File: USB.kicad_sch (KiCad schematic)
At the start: 37 parts, among them J1 USB_C_Receptacle_USB2.0_16P, U6 93AAxxBT-xOT, U7 USBLC6-2SC6, U8 FT4232H, Y2 Crystal_GND24

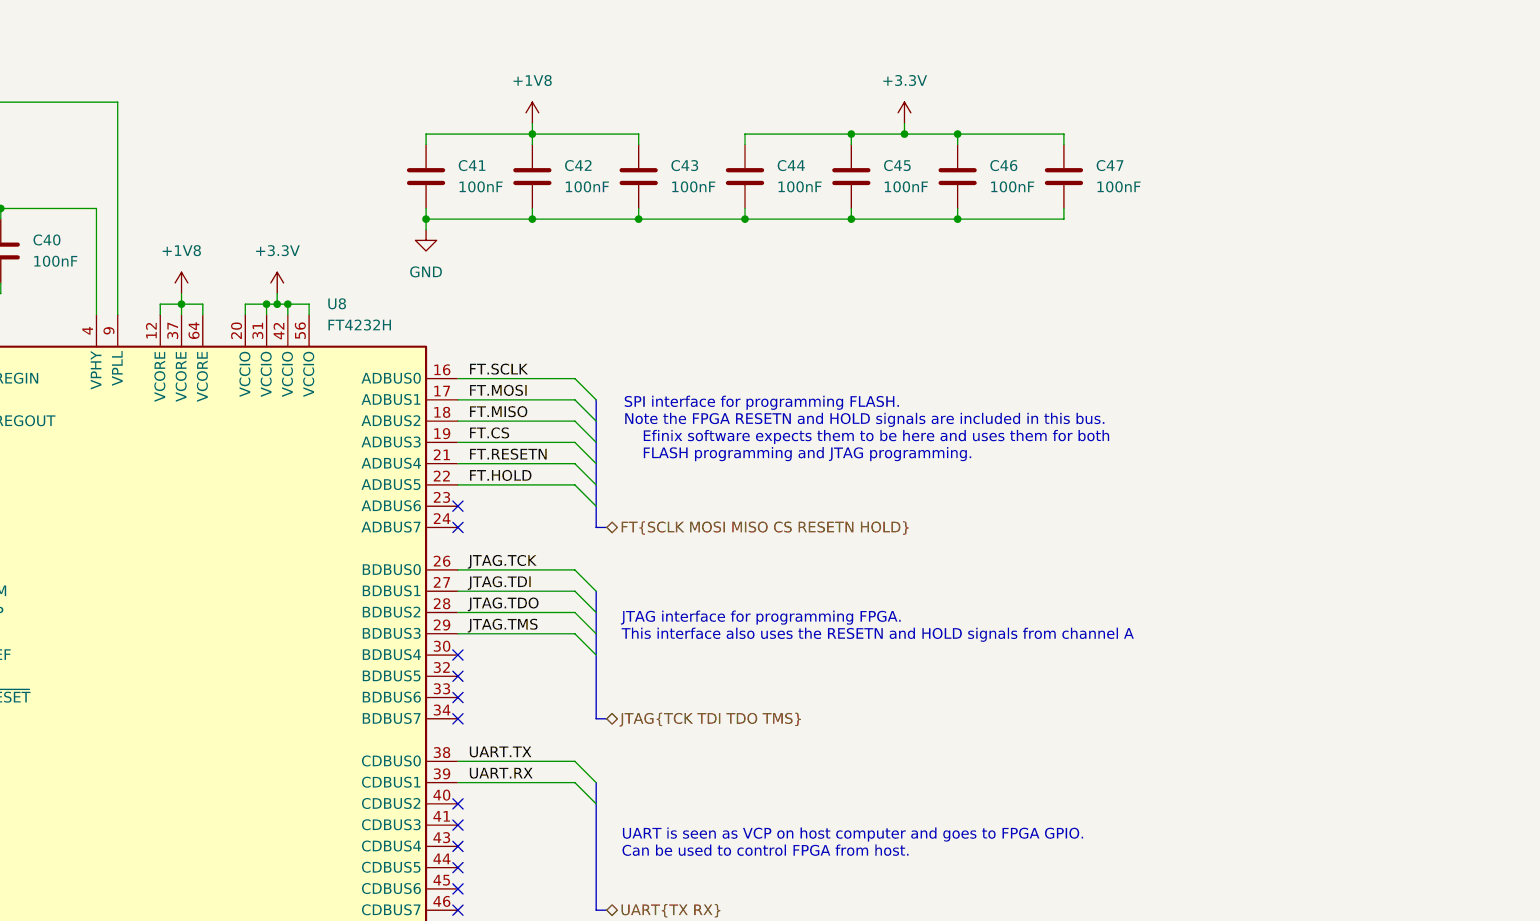
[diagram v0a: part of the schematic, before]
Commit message: Added SPI bus buffer
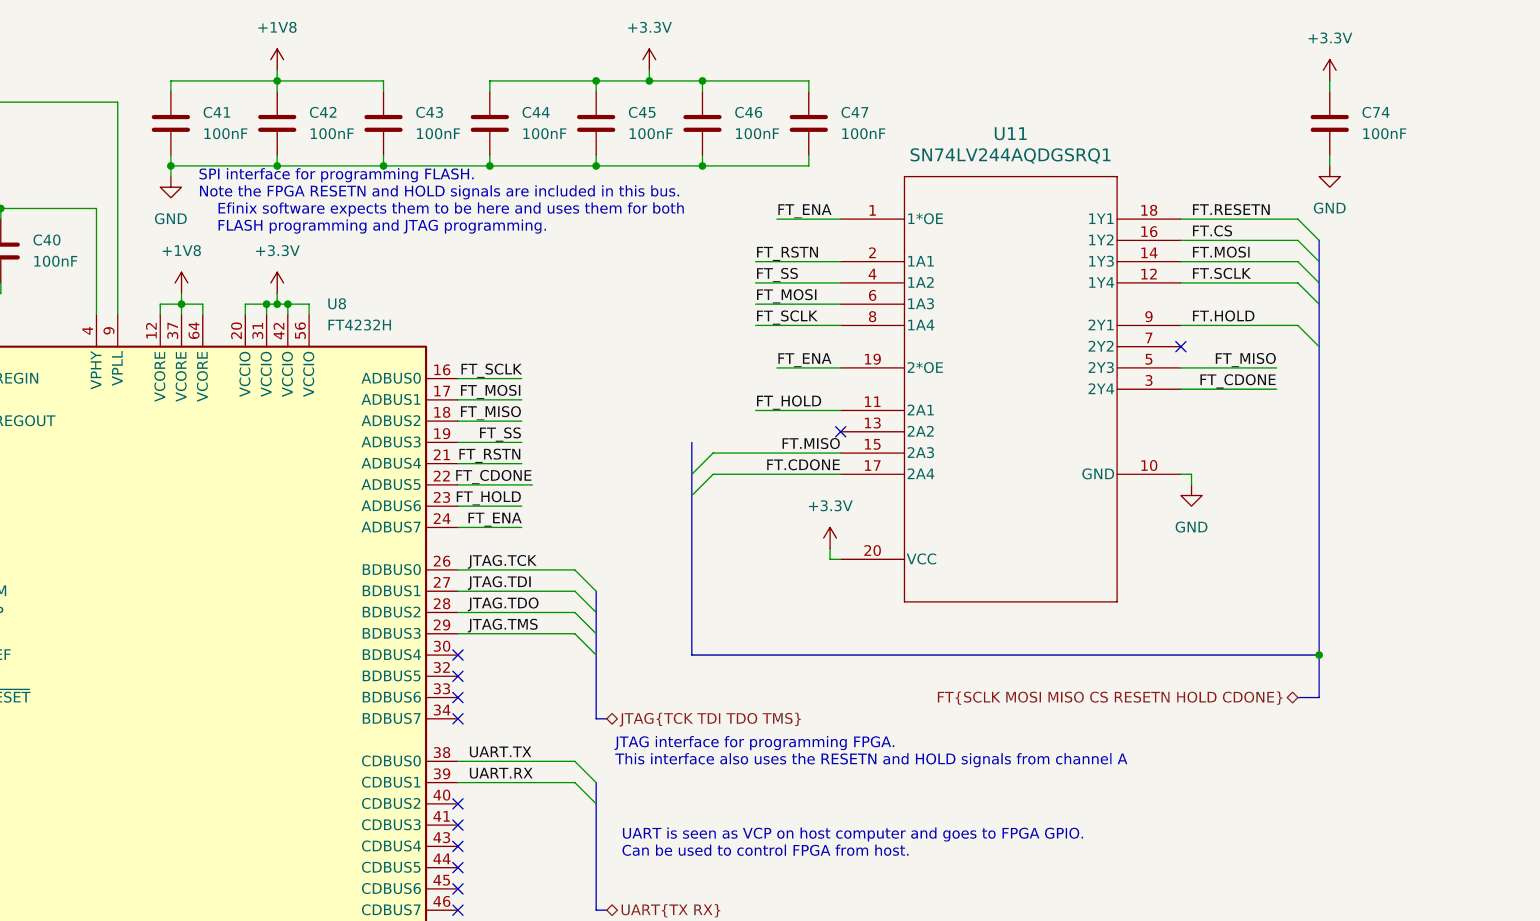
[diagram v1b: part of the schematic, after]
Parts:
- added C74: 100nF, Capacitor_SMD:C_0603_1608Metric, symbol Device:C
- added U11: SN74LV244AQDGSRQ1, SN74LV244AQDGSRQ1:VSSOP20_DGS_TEX, symbol SN74LV244AQDGSRQ1:SN74LV244AQDGSRQ1
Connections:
- net +3.3V: now also C74.1, U11.20 (VCC)
- net FT.CS: now also U11.16 (1Y2); no longer U8.19 (ADBUS3)
- net FT.HOLD: now also U11.9 (2Y1); no longer U8.22 (ADBUS5)
- net FT.MISO: now also U11.15 (2A3); no longer U8.18 (ADBUS2)
- net FT.MOSI: now also U11.14 (1Y3); no longer U8.17 (ADBUS1)
- net FT.RESETN: now also U11.18 (1Y1); no longer U8.21 (ADBUS4)
- net FT.SCLK: now also U11.12 (1Y4); no longer U8.16 (ADBUS0)
- net GND: now also C74.2, U11.10 (GND)
- net FT_HOLD: now reaches U8.23 (ADBUS6)
- net FT_HOLD: now also U11.11 (2A1)
- net FT_ENA: now reaches U8.24 (ADBUS7)
- net FT_ENA: now also U11.1 (1*OE), U11.19 (2*OE)
- new net FT.CDONE: U11.17 (2A4)
- new net FT_CDONE: U11.3 (2Y4), U8.22 (ADBUS5)
- new net FT_MISO: U11.5 (2Y3), U8.18 (ADBUS2)
- new net FT_MOSI: U11.6 (1A3), U8.17 (ADBUS1)
- new net FT_RSTN: U11.2 (1A1), U8.21 (ADBUS4)
- new net FT_SCLK: U11.8 (1A4), U8.16 (ADBUS0)
- new net FT_SS: U11.4 (1A2), U8.19 (ADBUS3)
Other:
- moved on the sheet: C41, C42, C43, C44, C45, C46, C47

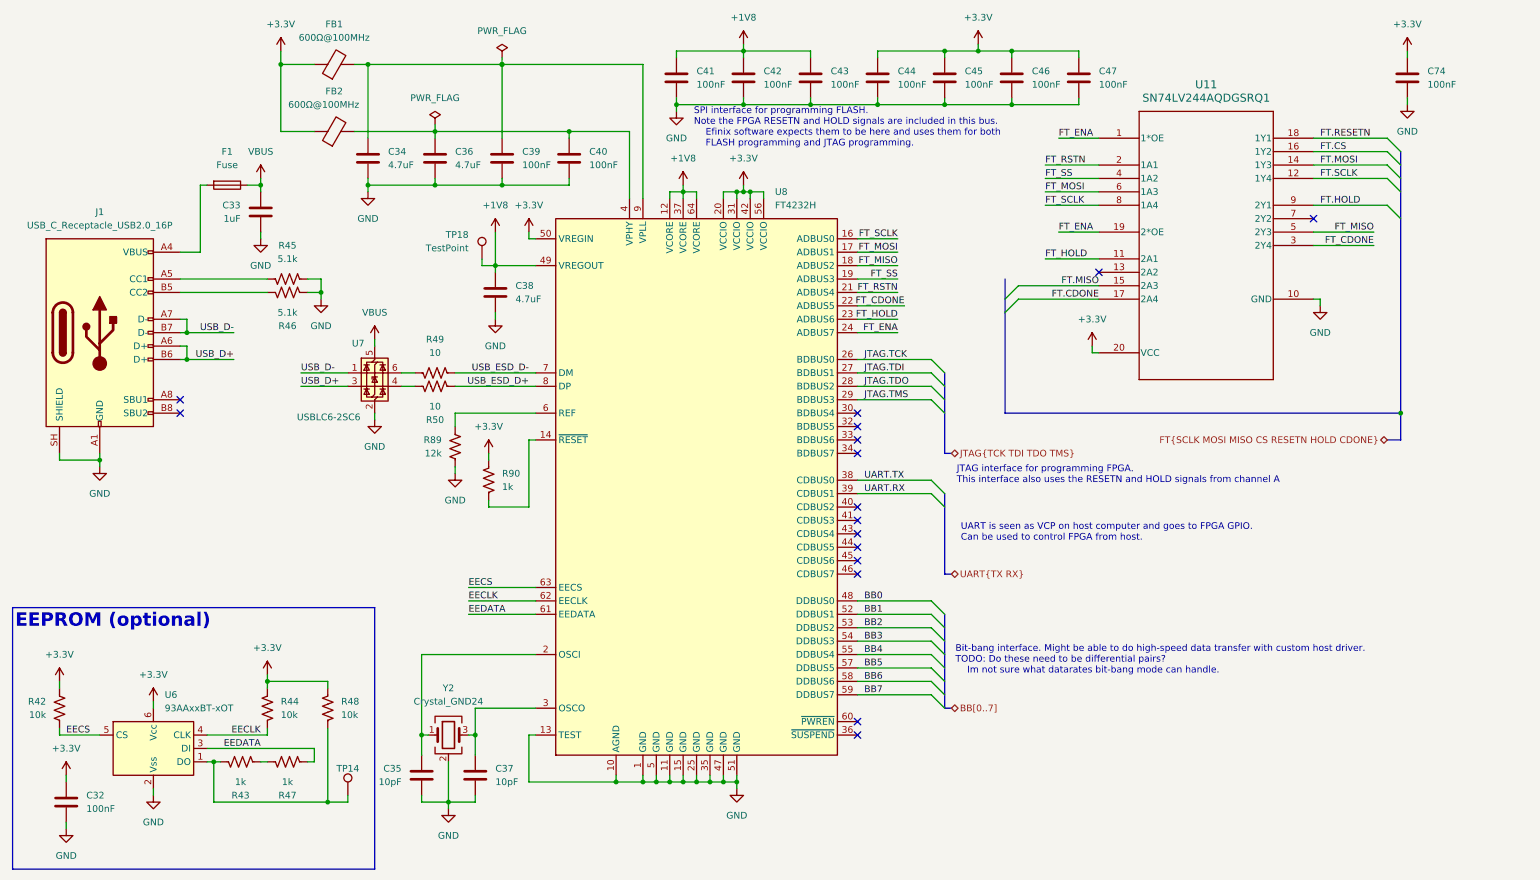
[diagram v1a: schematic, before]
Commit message: Added decal and gerbers
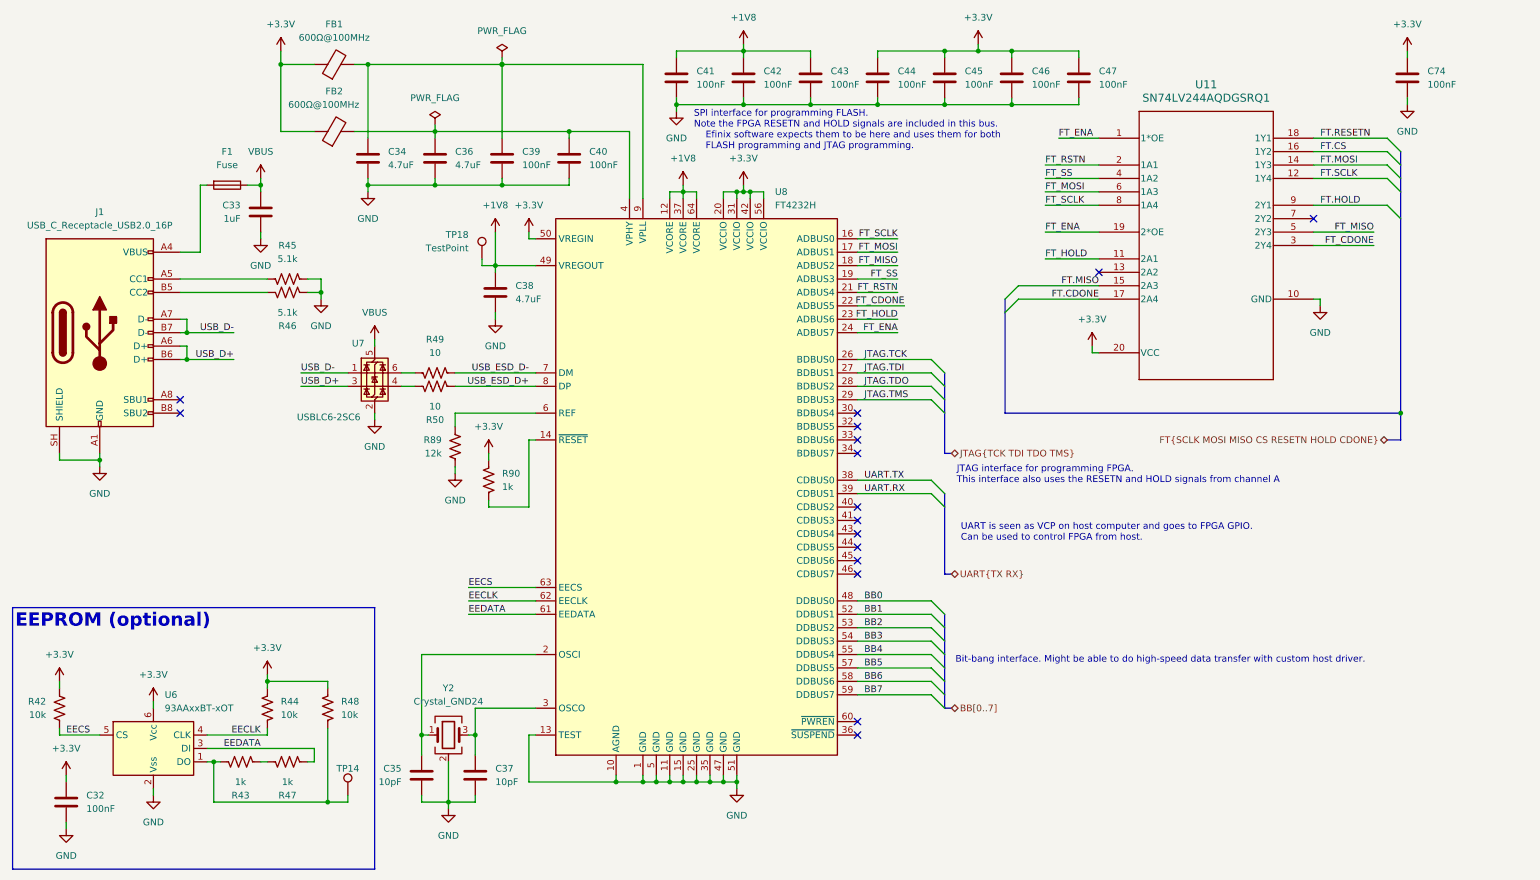
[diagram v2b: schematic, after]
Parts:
- U11: Digikey PN (none) -> 296-SN74LV244AQDGSRQ1CT-ND; Unit Cost (none) -> 0.68
- U7: Digikey PN (none) -> 497-5235-1-ND; Unit Cost (none) -> 0.54
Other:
- note added: "Bit-bang interface. Might be able to do high-speed data transfer with custom host driver."
- note removed: "Bit-bang interface. Might be able to do high-speed data transfer with custom host driver. TODO: Do these need to be differential pairs? Im not sure what datarates bit-bang mode can handle."
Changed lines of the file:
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@@
 	(text "SPI interface for programming FLASH.\nNote the FPGA RESETN and HOLD signals are included in this bus.\n	Efinix software expects them to be here and uses them for both \n	FLASH programming and JTAG programming."
 		(exclude_from_sim no)
-		(at 141.732 34.798 0)
+		(at 141.732 35.306 0)
 		(effects
 			(font
@@
 		)
 	)
-	(text "Bit-bang interface. Might be able to do high-speed data transfer with custom host driver.\nTODO: Do these need to be differential pairs? \n	Im not sure what datarates bit-bang mode can handle."
+	(text "Bit-bang interface. Might be able to do high-speed data transfer with custom host driver."
 		(exclude_from_sim no)
 		(at 191.262 135.636 0)
@@
 	(wire
 		(pts
-			(xy 80.01 22.86) (xy 105.41 22.86)
+			(xy 80.01 22.86) (xy 132.08 22.86)
 		)
 		(stroke
@@
 		)
 	)
-	(bus
+	(wire
 		(pts
-			(xy 200.66 63.5) (xy 200.66 88.9)
+			(xy 147.32 48.26) (xy 147.32 46.99)
 		)
 		(stroke
@@
 	(wire
 		(pts
-			(xy 147.32 48.26) (xy 147.32 46.99)
+			(xy 68.58 63.5) (xy 71.12 63.5)
 		)
 		(stroke
@@
 	(wire
 		(pts
-			(xy 68.58 63.5) (xy 71.12 63.5)
+			(xy 92.71 35.56) (xy 92.71 36.83)
 		)
 		(stroke
@@
 	(wire
 		(pts
-			(xy 92.71 35.56) (xy 92.71 36.83)
+			(xy 172.72 104.14) (xy 186.69 104.14)
 		)
 		(stroke
@@
 	(wire
 		(pts
-			(xy 172.72 104.14) (xy 186.69 104.14)
+			(xy 201.93 20.32) (xy 201.93 21.59)
 		)
 		(stroke
@@
 		)
 	)
-	(wire
+	(bus
 		(pts
-			(xy 201.93 20.32) (xy 201.93 21.59)
+			(xy 200.66 67.31) (xy 200.66 88.9)
 		)
 		(stroke
@@
 	(wire
 		(pts
-			(xy 210.82 54.61) (xy 218.44 54.61)
+			(xy 208.28 54.61) (xy 218.44 54.61)
 		)
 		(stroke
@@
 	(wire
 		(pts
-			(xy 105.41 22.86) (xy 132.08 22.86)
-		)
-		(stroke
-			(width 0)
-			(type default)
-		)
-	)
-	(wire
-		(pts
 			(xy 172.72 134.62) (xy 186.69 134.62)
 		)
@@
 	)
 	(label "FT_ENA"
-		(at 210.82 54.61 0)
+		(at 208.28 54.61 0)
 		(effects
 			(font
@@
 			)
 		)
+		(property "Digikey PN" "497-5235-1-ND"
+			(at 81.28 81.28 0)
+			(hide yes)
+			(show_name no)
+			(do_not_autoplace no)
+			(effects
+				(font
+					(size 1.27 1.27)
+				)
+			)
+		)
+		(property "Unit Cost" "0.54"
+			(at 81.28 81.28 0)
+			(hide yes)
+			(show_name no)
+			(do_not_autoplace no)
+			(effects
+				(font
+					(size 1.27 1.27)
+				)
+			)
+		)
 		(pin "3"
 		)
@@
 			(at 218.44 36.83 0)
 			(hide yes)
+			(show_name no)
+			(do_not_autoplace no)
+			(effects
+				(font
+					(size 1.27 1.27)
+				)
+			)
+		)
+		(property "Digikey PN" "296-SN74LV244AQDGSRQ1CT-ND"
+			(at 218.44 36.83 0)
+			(hide yes)
+			(show_name no)
+			(do_not_autoplace no)
+			(effects
+				(font
+					(size 1.27 1.27)
+				)
+			)
+		)
+		(property "Unit Cost" "0.68"
+			(at 218.44 36.83 0)
+			(hide yes)

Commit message: Finalized
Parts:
- C34, C36, C38: Digikey PN 1276-1044-1-ND -> 1276-1045-1-ND; Unit Cost 0.044 -> 0.041
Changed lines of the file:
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@@
 			)
 		)
-		(property "Digikey PN" "1276-1044-1-ND"
+		(property "Digikey PN" "1276-1045-1-ND"
 			(at 80.01 40.64 0)
 			(hide yes)
@@
 			)
 		)
-		(property "Unit Cost" "0.044"
+		(property "Unit Cost" "0.041"
 			(at 80.01 40.64 0)
 			(hide yes)
@@
 			)
 		)
-		(property "Digikey PN" "1276-1044-1-ND"
+		(property "Digikey PN" "1276-1045-1-ND"
 			(at 104.14 66.04 0)
 			(hide yes)
@@
 			)
 		)
-		(property "Unit Cost" "0.044"
+		(property "Unit Cost" "0.041"
 			(at 104.14 66.04 0)
 			(hide yes)
@@
 			)
 		)
-		(property "Digikey PN" "1276-1044-1-ND"
+		(property "Digikey PN" "1276-1045-1-ND"
 			(at 92.71 40.64 0)
 			(hide yes)
@@
 			)
 		)
-		(property "Unit Cost" "0.044"
+		(property "Unit Cost" "0.041"
 			(at 92.71 40.64 0)
 			(hide yes)
